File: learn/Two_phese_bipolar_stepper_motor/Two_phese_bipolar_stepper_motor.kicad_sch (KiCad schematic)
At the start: 28 parts, among them J1 Screw_Terminal_01x02, J4 Screw_Terminal_01x04

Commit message: 06/03/23 avanzamento corso...
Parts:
- gave numbers to parts that had none: 4
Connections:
- net GND: now also Rs1.2, Rs2.2, U2.8 (GND)
- net VS: now also U2.4 (Vs)
- net VSS: now also U2.9 (Vss)
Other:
- moved on the sheet: Rs1
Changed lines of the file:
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@@
   (junction (at 176.53 26.67) (diameter 0) (color 0 0 0 0)
   )
+  (junction (at 146.05 120.65) (diameter 0) (color 0 0 0 0)
+  )
   (junction (at 224.79 34.29) (diameter 0) (color 0 0 0 0)
   )
@@
     (stroke (width 0) (type default) (color 0 0 0 0))
   )
+  (wire (pts (xy 200.66 58.42) (xy 200.66 59.69))
+    (stroke (width 0) (type default) (color 0 0 0 0))
+  )
   (wire (pts (xy 191.77 25.4) (xy 191.77 26.67))
     (stroke (width 0) (type default) (color 0 0 0 0))
@@
     (stroke (width 0) (type default) (color 0 0 0 0))
   )
+  (wire (pts (xy 146.05 120.65) (xy 151.13 120.65))
+    (stroke (width 0) (type default) (color 0 0 0 0))
+  )
   (wire (pts (xy 220.98 72.39) (xy 255.27 72.39))
     (stroke (width 0) (type default) (color 0 0 0 0))
@@
     (stroke (width 0) (type default) (color 0 0 0 0))
   )
+  (wire (pts (xy 198.12 95.25) (xy 198.12 96.52))
+    (stroke (width 0) (type default) (color 0 0 0 0))
+  )
   (wire (pts (xy 187.96 36.83) (xy 187.96 39.37))
     (stroke (width 0) (type default) (color 0 0 0 0))
@@
     (stroke (width 0) (type default) (color 0 0 0 0))
   )
+  (wire (pts (xy 140.97 120.65) (xy 146.05 120.65))
+    (stroke (width 0) (type default) (color 0 0 0 0))
+  )
   (wire (pts (xy 220.98 72.39) (xy 220.98 85.09))
     (stroke (width 0) (type default) (color 0 0 0 0))
@@
     (stroke (width 0) (type default) (color 0 0 0 0))
   )
+  (wire (pts (xy 198.12 58.42) (xy 198.12 59.69))
+    (stroke (width 0) (type default) (color 0 0 0 0))
+  )
   (wire (pts (xy 243.84 82.55) (xy 243.84 85.09))
     (stroke (width 0) (type default) (color 0 0 0 0))
@@
   )
   (wire (pts (xy 215.9 34.29) (xy 224.79 34.29))
+    (stroke (width 0) (type default) (color 0 0 0 0))
+  )
+  (wire (pts (xy 146.05 120.65) (xy 146.05 123.19))
     (stroke (width 0) (type default) (color 0 0 0 0))
   )
@@
   (symbol (lib_id "Device:R") (at 140.97 116.84 0) (unit 1)
     (in_bom yes) (on_board yes) (fields_autoplaced)
-    (property "Reference" "R?" (id 0) (at 143.51 115.5699 0)
+    (property "Reference" "Rs2" (id 0) (at 143.51 115.5699 0)
       (effects (font (size 1.27 1.27)) (justify left))
     )
@@
     (pin "1")
     (pin "2")
+  )
+  (symbol (lib_id "power:VSS") (at 198.12 58.42 0) (unit 1)
+    (in_bom yes) (on_board yes)
+    (property "Reference" "#PWR?" (id 0) (at 198.12 62.23 0)
+      (effects (font (size 1.27 1.27)) hide)
+    )
+    (property "Value" "VSS" (id 1) (at 196.85 54.61 0)
+      (effects (font (size 0.9 0.9)) (justify left))
+    )
+    (property "Footprint" "" (id 2) (at 198.12 58.42 0)
+      (effects (font (size 1.27 1.27)) hide)
+    )
+    (property "Datasheet" "" (id 3) (at 198.12 58.42 0)
+      (effects (font (size 1.27 1.27)) hide)
+    )
+    (pin "1")
   )
   (symbol (lib_id "power:GND") (at 187.96 39.37 0) (unit 1)
@@
     )
     (property "Datasheet" "" (id 3) (at 187.96 39.37 0)
+      (effects (font (size 1.27 1.27)) hide)
+    )
+    (pin "1")
+  )
+  (symbol (lib_id "power:VS") (at 200.66 58.42 0) (unit 1)
+    (in_bom yes) (on_board yes)
+    (property "Reference" "#PWR?" (id 0) (at 195.58 62.23 0)
+      (effects (font (size 1.27 1.27)) hide)
+    )
+    (property "Value" "VS" (id 1) (at 200.66 54.61 0)
+      (effects (font (size 0.9 0.9)) (justify left))
+    )
+    (property "Footprint" "" (id 2) (at 200.66 58.42 0)
+      (effects (font (size 1.27 1.27)) hide)
+    )
+    (property "Datasheet" "" (id 3) (at 200.66 58.42 0)
       (effects (font (size 1.27 1.27)) hide)
     )
@@
     (pin "2")
   )
+  (symbol (lib_id "power:GND") (at 198.12 96.52 0) (unit 1)
+    (in_bom yes) (on_board yes) (fields_autoplaced)
+    (property "Reference" "#PWR?" (id 0) (at 198.12 102.87 0)
+      (effects (font (size 1.27 1.27)) hide)
+    )
+    (property "Value" "GND" (id 1) (at 198.12 101.6 0))
+    (property "Footprint" "" (id 2) (at 198.12 96.52 0)
+      (effects (font (size 1.27 1.27)) hide)
+    )
+    (property "Datasheet" "" (id 3) (at 198.12 96.52 0)
+      (effects (font (size 1.27 1.27)) hide)
+    )
+    (pin "1")
+  )
   (symbol (lib_id "power:GND") (at 232.41 95.25 0) (unit 1)
     (in_bom yes) (on_board yes) (fields_autoplaced)
@@
     (pin "1")
   )
-  (symbol (lib_id "Device:R") (at 149.86 116.84 0) (unit 1)
-    (in_bom yes) (on_board yes) (fields_autoplaced)
-    (property "Reference" "R?" (id 0) (at 152.4 115.5699 0)
-      (effects (font (size 1.27 1.27)) (justify left))
-    )
-    (property "Value" "R" (id 1) (at 152.4 118.1099 0)
-      (effects (font (size 1.27 1.27)) (justify left))
-    )
-    (property "Footprint" "" (id 2) (at 148.082 116.84 90)
-      (effects (font (size 1.27 1.27)) hide)
-    )
-    (property "Datasheet" "~" (id 3) (at 149.86 116.84 0)
+  (symbol (lib_id "Device:R") (at 151.13 116.84 0) (unit 1)
+    (in_bom yes) (on_board yes) (fields_autoplaced)
+    (property "Reference" "Rs1" (id 0) (at 153.67 115.5699 0)
+      (effects (font (size 1.27 1.27)) (justify left))
+    )
+    (property "Value" "R" (id 1) (at 153.67 118.1099 0)
+      (effects (font (size 1.27 1.27)) (justify left))
+    )
+    (property "Footprint" "" (id 2) (at 149.352 116.84 90)
+      (effects (font (size 1.27 1.27)) hide)
+    )
+    (property "Datasheet" "~" (id 3) (at 151.13 116.84 0)
       (effects (font (size 1.27 1.27)) hide)
     )
@@
     (pin "2")
   )
+  (symbol (lib_id "power:GND") (at 146.05 123.19 0) (unit 1)
+    (in_bom yes) (on_board yes) (fields_autoplaced)
+    (property "Reference" "#PWR?" (id 0) (at 146.05 129.54 0)
+      (effects (font (size 1.27 1.27)) hide)
+    )
+    (property "Value" "GND" (id 1) (at 146.05 128.27 0))
+    (property "Footprint" "" (id 2) (at 146.05 123.19 0)
+      (effects (font (size 1.27 1.27)) hide)
+    )
+    (property "Datasheet" "" (id 3) (at 146.05 123.19 0)
+      (effects (font (size 1.27 1.27)) hide)
+    )
+    (pin "1")
+  )
   (symbol (lib_id "power:GND") (at 224.79 36.83 0) (unit 1)
     (in_bom yes) (on_board yes) (fields_autoplaced)
@@
   (symbol (lib_id "Driver_Motor:L297") (at 73.66 135.89 0) (unit 1)
     (in_bom yes) (on_board yes) (fields_autoplaced)
-    (property "Reference" "U?" (id 0) (at 75.6794 153.67 0)
+    (property "Reference" "U1" (id 0) (at 75.6794 153.67 0)
       (effects (font (size 1.27 1.27)) (justify left))
     )
@@
   (symbol (lib_id "Driver_Motor:L298N") (at 198.12 77.47 0) (unit 1)
     (in_bom yes) (on_board yes) (fields_autoplaced)
-    (property "Reference" "U?" (id 0) (at 202.6794 57.15 0)
+    (property "Reference" "U2" (id 0) (at 202.6794 57.15 0)
       (effects (font (size 1.27 1.27)) (justify left))
     )
@@
       (reference "#FLG?") (unit 1) (value "PWR_FLAG") (footprint "")
     )
+    (path "/2bf7e311-f4f2-4486-9479-5705f7bd3f8c"
+      (reference "#PWR?") (unit 1) (value "VSS") (footprint "")
+    )
     (path "/2c34f367-ff20-455d-af43-7cdb3c218d3c"
       (reference "#PWR?") (unit 1) (value "GND") (footprint "")
     )
+    (path "/300d980e-972c-45f8-9507-49062df70e8e"
+      (reference "#PWR?") (unit 1) (value "VS") (footprint "")
+    )
+    (path "/5778c62f-577d-4fa9-8c82-efee9849e4b5"
+      (reference "#PWR?") (unit 1) (value "GND") (footprint "")
+    )
     (path "/581caf96-d5c9-4257-a3b2-00f1f50eba58"
       (reference "#PWR?") (unit 1) (value "GND") (footprint "")
@@
       (reference "#PWR?") (unit 1) (value "VSS") (footprint "")
     )
+    (path "/a79b088c-2e4f-4f5f-9dd1-ccabd55730b5"
+      (reference "#PWR?") (unit 1) (value "GND") (footprint "")
+    )
     (path "/a9f14768-0b91-4847-9866-5d52c398adaf"
       (reference "#PWR?") (unit 1) (value "GND") (footprint "")
@@
       (reference "R1") (unit 1) (value "22k") (footprint "")
     )
+    (path "/810f6ba5-70c4-4553-b4e3-ea0dba905cbb"
+      (reference "Rs1") (unit 1) (value "R") (footprint "")
+    )
     (path "/1f67e1ec-5130-416c-91d7-a47e17e20ec0"
-      (reference "R?") (unit 1) (value "R") (footprint "")
-    )
-    (path "/810f6ba5-70c4-4553-b4e3-ea0dba905cbb"
-      (reference "R?") (unit 1) (value "R") (footprint "")
+      (reference "Rs2") (unit 1) (value "R") (footprint "")
     )
     (path "/b420444f-520c-4962-ac46-908b94e46b38"
-      (reference "U?") (unit 1) (value "L297") (footprint "")
+      (reference "U1") (unit 1) (value "L297") (footprint "")
     )
     (path "/e37ffe64-a844-4622-840a-a53a0744ab08"
-      (reference "U?") (unit 1) (value "L298N") (footprint "Package_TO_SOT_THT:TO-220-15_P2.54x2.54mm_StaggerOdd_Lead4.58mm_Vertical")
-    )
-  )
+      (reference "U2") (unit 1) (value "L298N") (footprint "Package_TO_SOT_THT:TO-220-15_P2.54x2.54mm_StaggerOdd_Lead4.58mm_Vertical")
+    )
+  )

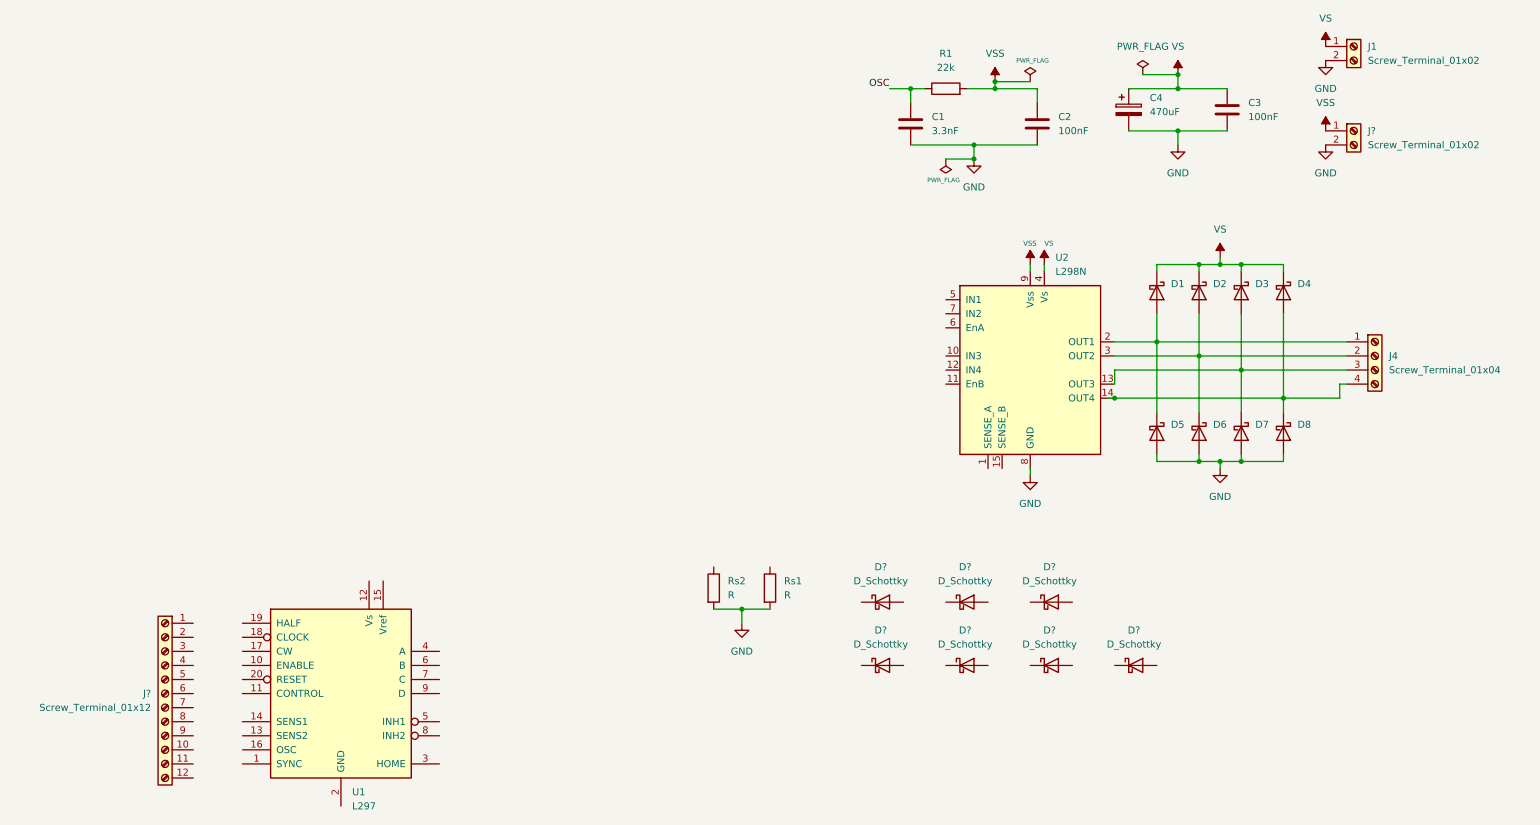
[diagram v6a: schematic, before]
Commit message: Inizio collegamento L297 con L298N
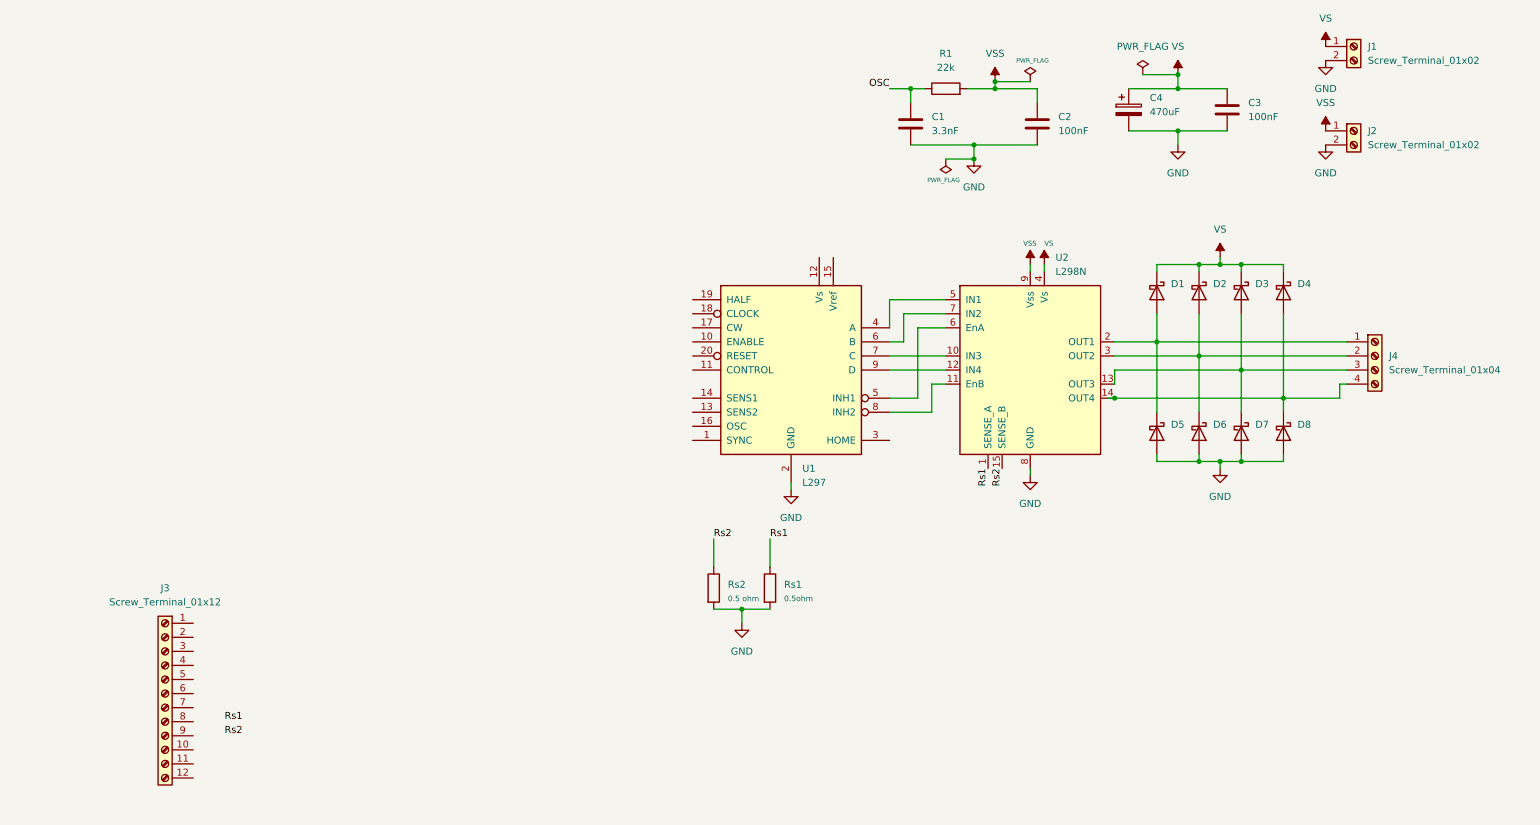
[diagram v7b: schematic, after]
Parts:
- removed D? (x7): D_Schottky, symbol Device:D_Schottky
- Rs1: value R -> 0.5ohm
- Rs2: value R -> 0.5 ohm
- gave numbers to parts that had none: 2
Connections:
- net GND: now also U1.2 (GND)
- net Rs2: now reaches Rs2.1
- net Rs2: now also U2.15 (SENSE_B)
- net Rs1: now reaches Rs1.1
- net Rs1: now also U2.1 (SENSE_A)
- net at U1.4 (A): now also U2.5 (IN1)
- net at U1.5 (INH1): now also U2.6 (EnA)
- net at U1.6 (B): now also U2.7 (IN2)
- net at U1.7 (C): now also U2.10 (IN3)
- net at U1.8 (INH2): now also U2.11 (EnB)
- net at U1.9 (D): now also U2.12 (IN4)
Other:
- moved on the sheet: U1

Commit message: Avanzamento corso....
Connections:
- net GND: now also J3.1 (Pin_1)
- net OSC: now also J3.10 (Pin_10), U1.16 (OSC)
- net Rs1: now also U1.14 (SENS1)
- net Rs2: now also U1.13 (SENS2)
- net VSS: now also U1.12 (Vs)
- net SYNC: now reaches J3.11 (Pin_11)
- net SYNC: now also U1.1 (SYNC)
- net HALF: now reaches J3.2 (Pin_2)
- net HALF: now also U1.19 (HALF)
- net HOME: now reaches J3.3 (Pin_3)
- net HOME: now also U1.3 (HOME)
- net Vref: now reaches J3.4 (Pin_4)
- net Vref: now also U1.15 (Vref)
- net CLK: now reaches J3.5 (Pin_5)
- net CLK: now also U1.18 (CLOCK)
- net CW: now reaches J3.6 (Pin_6)
- net CW: now also U1.17 (CW)
- net ENA: now reaches J3.7 (Pin_7)
- net ENA: now also U1.10 (ENABLE)
- net RESET: now reaches J3.8 (Pin_8)
- net RESET: now also U1.20 (RESET)
- net CTRL: now reaches J3.9 (Pin_9)
- net CTRL: now also U1.11 (CONTROL)
- no-connect marks 0 -> 1
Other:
- moved on the sheet: J3
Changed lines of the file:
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@@
   (junction (at 187.96 36.83) (diameter 0) (color 0 0 0 0)
   )
+  (no_connect (at 114.3 92.71))
   (wire (pts (xy 228.6 58.42) (xy 232.41 58.42))
     (stroke (width 0) (type default) (color 0 0 0 0))
@@
     (stroke (width 0) (type default) (color 0 0 0 0))
   )
+  (wire (pts (xy 114.3 64.77) (xy 123.19 64.77))
+    (stroke (width 0) (type default) (color 0 0 0 0))
+  )
   (wire (pts (xy 224.79 26.67) (xy 233.68 26.67))
     (stroke (width 0) (type default) (color 0 0 0 0))
@@
     (stroke (width 0) (type default) (color 0 0 0 0))
   )
-  (label "Rs1" (at 55.88 140.97 180)
+  (label "Rs1" (at 137.16 82.55 180)
+    (effects (font (size 1.27 1.27)) (justify right bottom))
+  )
+  (label "ENA" (at 137.16 72.39 180)
     (effects (font (size 1.27 1.27)) (justify right bottom))
   )
@@
     (effects (font (size 1.27 1.27)) (justify left bottom))
   )
+  (label "OSC" (at 114.3 87.63 0)
+    (effects (font (size 1.27 1.27)) (justify left bottom))
+  )
+  (label "OSC" (at 137.16 87.63 180)
+    (effects (font (size 1.27 1.27)) (justify right bottom))
+  )
+  (label "CLK" (at 137.16 67.31 180)
+    (effects (font (size 1.27 1.27)) (justify right bottom))
+  )
+  (label "CTRL" (at 114.3 85.09 0)
+    (effects (font (size 1.27 1.27)) (justify left bottom))
+  )
   (label "OSC" (at 172.72 26.67 180)
     (effects (font (size 1.27 1.27)) (justify right bottom))
   )
+  (label "HOME" (at 172.72 90.17 0)
+    (effects (font (size 1.27 1.27)) (justify left bottom))
+  )
   (label "Rs2" (at 140.97 107.95 0)
     (effects (font (size 1.27 1.27)) (justify left bottom))
   )
-  (label "Rs2" (at 55.88 143.51 180)
-    (effects (font (size 1.27 1.27)) (justify right bottom))
+  (label "SYNC" (at 137.16 90.17 180)
+    (effects (font (size 1.27 1.27)) (justify right bottom))
+  )
+  (label "HOME" (at 114.3 69.85 0)
+    (effects (font (size 1.27 1.27)) (justify left bottom))
+  )
+  (label "Vref" (at 114.3 72.39 0)
+    (effects (font (size 1.27 1.27)) (justify left bottom))
+  )
+  (label "ENA" (at 114.3 80.01 0)
+    (effects (font (size 1.27 1.27)) (justify left bottom))
+  )
+  (label "Rs2" (at 137.16 85.09 180)
+    (effects (font (size 1.27 1.27)) (justify right bottom))
+  )
+  (label "Vref" (at 162.56 57.15 0)
+    (effects (font (size 1 1)) (justify left bottom))
   )
   (label "Rs2" (at 193.04 95.25 270)
     (effects (font (size 1.27 1.27)) (justify right bottom))
   )
+  (label "CW" (at 137.16 69.85 180)
+    (effects (font (size 1.27 1.27)) (justify right bottom))
+  )
+  (label "SYNC" (at 114.3 90.17 0)
+    (effects (font (size 1.27 1.27)) (justify left bottom))
+  )
+  (label "CLK" (at 114.3 74.93 0)
+    (effects (font (size 1.27 1.27)) (justify left bottom))
+  )
+  (label "HALF" (at 114.3 67.31 0)
+    (effects (font (size 1.27 1.27)) (justify left bottom))
+  )
+  (label "RESET" (at 114.3 82.55 0)
+    (effects (font (size 1.27 1.27)) (justify left bottom))
+  )
+  (label "RESET" (at 137.16 74.93 180)
+    (effects (font (size 1.27 1.27)) (justify right bottom))
+  )
+  (label "HALF" (at 137.16 64.77 180)
+    (effects (font (size 1.27 1.27)) (justify right bottom))
+  )
+  (label "CW" (at 114.3 77.47 0)
+    (effects (font (size 1.27 1.27)) (justify left bottom))
+  )
   (label "Rs1" (at 190.5 95.25 270)
     (effects (font (size 1.27 1.27)) (justify right bottom))
   )
+  (label "CTRL" (at 137.16 77.47 180)
+    (effects (font (size 1.27 1.27)) (justify right bottom))
+  )
   (symbol (lib_id "Device:D_Schottky") (at 243.84 63.5 270) (unit 1)
     (in_bom yes) (on_board yes) (fields_autoplaced)
@@
     (pin "2")
   )
-  (symbol (lib_id "Connector:Screw_Terminal_01x12") (at 41.91 135.89 0) (mirror y) (unit 1)
-    (in_bom yes) (on_board yes) (fields_autoplaced)
-    (property "Reference" "J3" (id 0) (at 41.91 116.84 0))
-    (property "Value" "Screw_Terminal_01x12" (id 1) (at 41.91 119.38 0))
-    (property "Footprint" "" (id 2) (at 41.91 135.89 0)
-      (effects (font (size 1.27 1.27)) hide)
-    )
-    (property "Datasheet" "~" (id 3) (at 41.91 135.89 0)
+  (symbol (lib_id "Connector:Screw_Terminal_01x12") (at 109.22 77.47 0) (mirror y) (unit 1)
+    (in_bom yes) (on_board yes) (fields_autoplaced)
+    (property "Reference" "J3" (id 0) (at 109.22 58.42 0))
+    (property "Value" "Screw_Terminal_01x12" (id 1) (at 109.22 60.96 0))
+    (property "Footprint" "" (id 2) (at 109.22 77.47 0)
+      (effects (font (size 1.27 1.27)) hide)
+    )
+    (property "Datasheet" "~" (id 3) (at 109.22 77.47 0)
       (effects (font (size 1.27 1.27)) hide)
     )
@@
     (pin "1")
   )
+  (symbol (lib_id "power:GND") (at 123.19 64.77 0) (unit 1)
+    (in_bom yes) (on_board yes) (fields_autoplaced)
+    (property "Reference" "#PWR0117" (id 0) (at 123.19 71.12 0)
+      (effects (font (size 1.27 1.27)) hide)
+    )
+    (property "Value" "GND" (id 1) (at 123.19 69.85 0))
+    (property "Footprint" "" (id 2) (at 123.19 64.77 0)
+      (effects (font (size 1.27 1.27)) hide)
+    )
+    (property "Datasheet" "" (id 3) (at 123.19 64.77 0)
+      (effects (font (size 1.27 1.27)) hide)
+    )
+    (pin "1")
+  )
   (symbol (lib_id "power:GND") (at 251.46 21.59 0) (unit 1)
     (in_bom yes) (on_board yes) (fields_autoplaced)
@@
     (pin "1")
   )
+  (symbol (lib_id "power:VSS") (at 160.02 57.15 0) (unit 1)
+    (in_bom yes) (on_board yes)
+    (property "Reference" "#PWR0115" (id 0) (at 160.02 60.96 0)
+      (effects (font (size 1.27 1.27)) hide)
+    )
+    (property "Value" "VSS" (id 1) (at 158.75 53.34 0)
+      (effects (font (size 0.9 0.9)) (justify left))
+    )
+    (property "Footprint" "" (id 2) (at 160.02 57.15 0)
+      (effects (font (size 1.27 1.27)) hide)
+    )
+    (property "Datasheet" "" (id 3) (at 160.02 57.15 0)
+      (effects (font (size 1.27 1.27)) hide)
+    )
+    (pin "1")
+  )
   (symbol (lib_id "Device:D_Schottky") (at 220.98 63.5 270) (unit 1)
     (in_bom yes) (on_board yes) (fields_autoplaced)
@@
   (symbol (lib_id "power:GND") (at 154.94 99.06 0) (unit 1)
     (in_bom yes) (on_board yes) (fields_autoplaced)
-    (property "Reference" "#PWR?" (id 0) (at 154.94 105.41 0)
+    (property "Reference" "#PWR0116" (id 0) (at 154.94 105.41 0)
       (effects (font (size 1.27 1.27)) hide)
     )
@@
       (reference "#PWR0114") (unit 1) (value "GND") (footprint "")
     )
+    (path "/8eeab5cb-6893-4264-a43c-df8906e817db"
+      (reference "#PWR0115") (unit 1) (value "VSS") (footprint "")
+    )
     (path "/9b035954-a727-4e80-a396-cf2f726a3998"
-      (reference "#PWR?") (unit 1) (value "GND") (footprint "")
+      (reference "#PWR0116") (unit 1) (value "GND") (footprint "")
+    )
+    (path "/7aaf0490-6132-440f-b152-239c8904f720"
+      (reference "#PWR0117") (unit 1) (value "GND") (footprint "")
     )
     (path "/c05e48eb-bbb9-4101-8804-a57500110c23"
